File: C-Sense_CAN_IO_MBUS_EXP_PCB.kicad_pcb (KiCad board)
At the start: 4 copper layers, 52 x 65 mm, 81 parts, among them IC1 SC16IS750IBS_128, J1 Conn_01x10_Female, J2 Conn_01x04_Female, J214 Conn_01x02_Male, J215 Conn_01x03_Male, J216 Conn_01x02_Male, J220 Conn_01x02_Male, J221 Conn_01x03_Male, J3 Conn_01x06_Female, J4 SJ1-3533NG, Q1 BSN20, Q1602 BSN20, Q2402 BC337, Q2403 BC337, Q2404 BD136, U1 LTV-817, U1701 LTV-817, U2 AZ34063U, U3 LTV-817, U4 LTV-817, Y1 OSC 1.8432

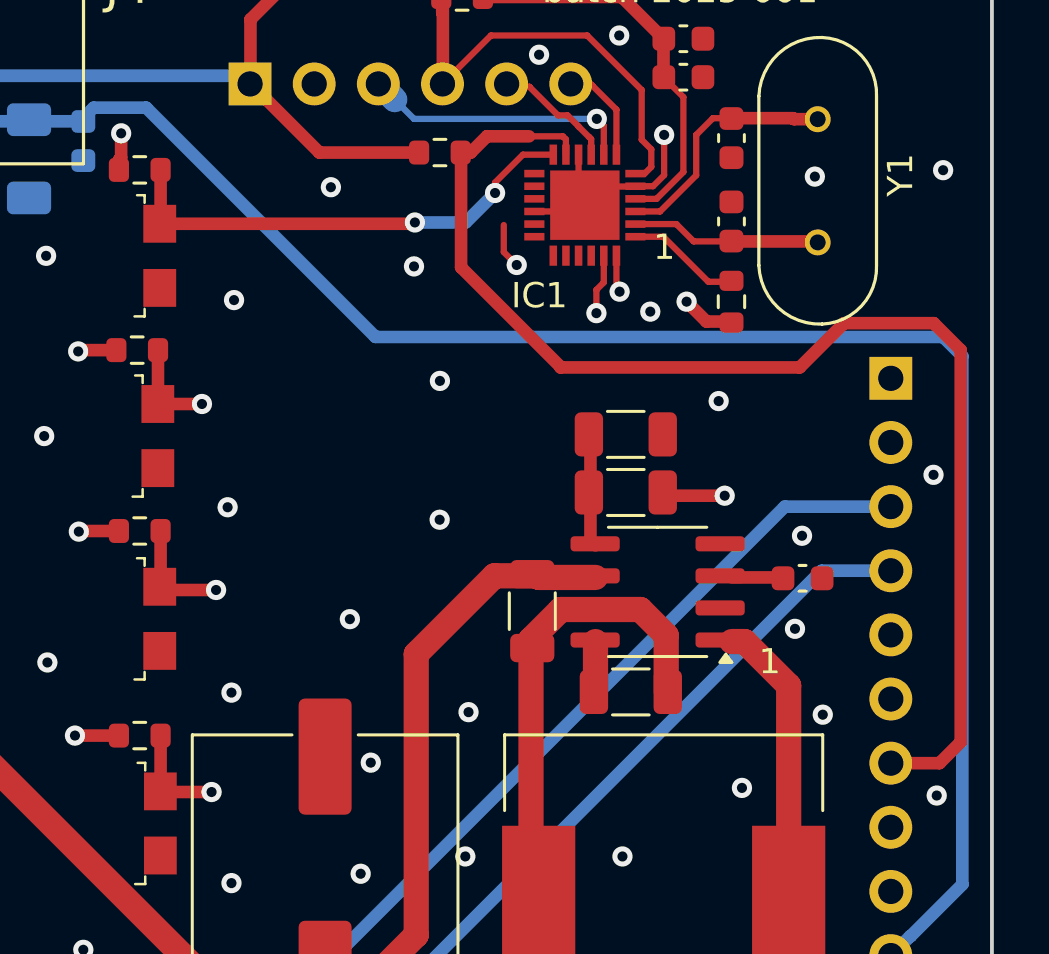
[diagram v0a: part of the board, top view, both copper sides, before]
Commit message: changed pin of digital in 1 to a GPIO to be able to handel a serial connection
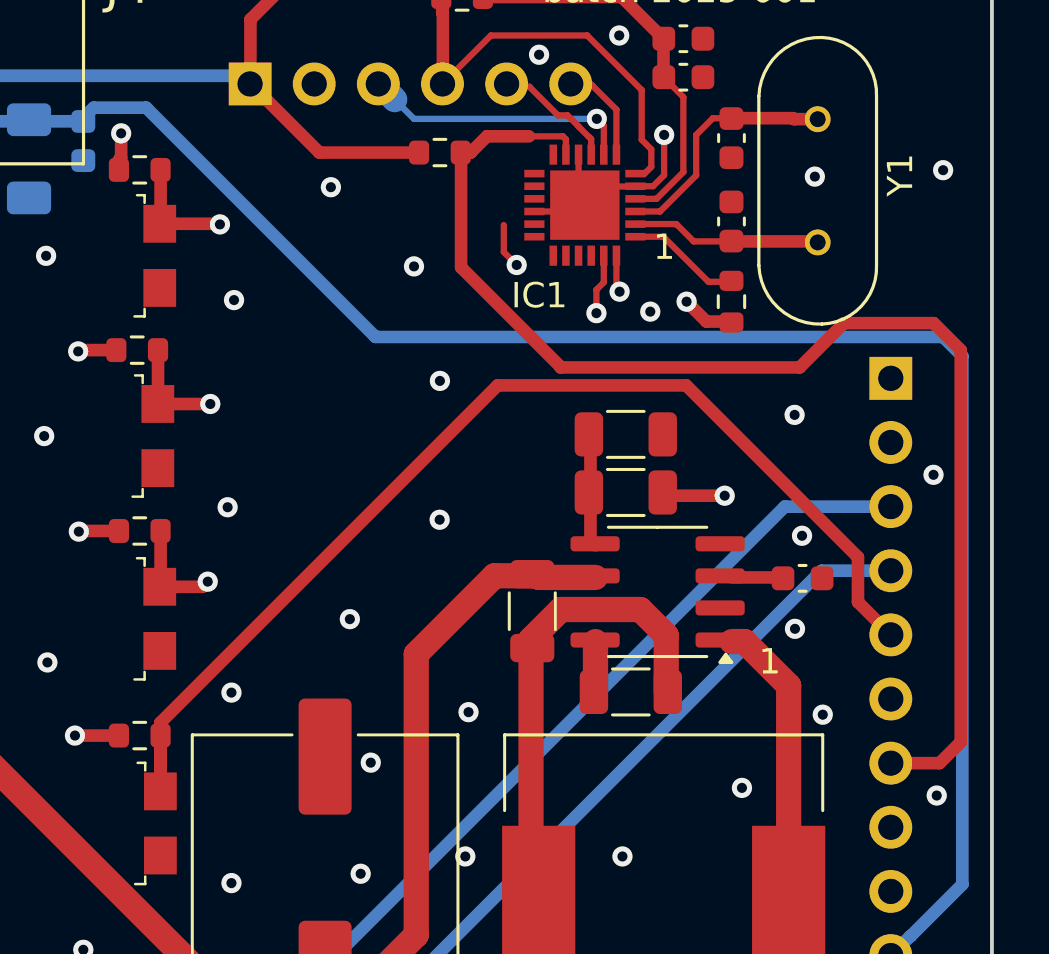
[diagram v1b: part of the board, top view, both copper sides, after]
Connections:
- IC1 pad 12: /Master_PCB/SPI_UART_GPIO_0 -> /Master_PCB/SPI-UART/GPIO_0
- R1702 pad 2: /Master_PCB/MP_Dig1_EXP -> /Master_PCB/GPIO_35_EXP
- R4 pad 2: /Master_PCB/SPI_UART_GPIO_0 -> /Master_PCB/MP_Dig4_EXP
- R6 pad 2: /Master_PCB/MP_Dig4_EXP -> /Master_PCB/MP_Dig2_EXP
- R8 pad 2: /Master_PCB/MP_Dig2_EXP -> /Master_PCB/MP_Dig1_EXP
- U1 pad 4: /Master_PCB/SPI_UART_GPIO_0 -> /Master_PCB/MP_Dig4_EXP
- U1701 pad 4: /Master_PCB/MP_Dig1_EXP -> /Master_PCB/GPIO_35_EXP
- U3 pad 4: /Master_PCB/MP_Dig4_EXP -> /Master_PCB/MP_Dig2_EXP
- U4 pad 4: /Master_PCB/MP_Dig2_EXP -> /Master_PCB/MP_Dig1_EXP
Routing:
- net /Master_PCB/GPIO_35_EXP: track 0.00 -> 44.6 mm
- net /Master_PCB/SPI_UART_GPIO_0: track 19.1 -> 0.00 mm, vias 2 -> 0
- net /Master_PCB/MP_Dig1_EXP: track 32.8 -> 36.5 mm
- net /Master_PCB/MP_Dig2_EXP: track 35.1 -> 38.1 mm
- net /Master_PCB/MP_Dig4_EXP: track 36.0 -> 38.9 mm
